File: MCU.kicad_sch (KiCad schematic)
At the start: 101 parts, among them J301 I2C1, J302 I2C4, U301 MICROCONTROLLER, X301 25MHz 8pF

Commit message: starting to incorporate todos
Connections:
- net TX_PWM_A: now also U301.H12 (PD14); no longer U301.F11 (PC7)
- net TX_PWM_B: now also U301.H11 (PD12); no longer U301.D11 (PH14)
- no-connect marks 69 -> 68
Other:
- moved on the sheet: TP357, TP366

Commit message: slight tweaks
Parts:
- added TP304: TP_ROUND_TH_300um, BR_Virtual_Parts:TP_ROUND_SMT_300um, symbol BR_Virtual_Parts:TP_ROUND_SMT_300um
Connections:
- net TX_PWM_A: now also TP357.1, U301.H11 (PD12); no longer TP366.1, U301.H12 (PD14)
- net TX_PWM_B: now also TP366.1, U301.H12 (PD14); no longer TP357.1, U301.H11 (PD12)
- net DEBUG1: now reaches U301.G10 (PD15)
- net DEBUG1: now also TP304.1
- no-connect marks 68 -> 67
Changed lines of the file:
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@@
 	)
 	(junction
+		(at 256.54 332.74)
+		(diameter 0)
+		(color 0 0 0 0)
+	)
+	(junction
 		(at 140.97 46.99)
 		(diameter 0)
@@
 	)
 	(no_connect
-		(at 231.14 332.74)
-	)
-	(no_connect
 		(at 157.48 203.2)
 	)
@@
 	(wire
 		(pts
+			(xy 231.14 332.74) (xy 256.54 332.74)
+		)
+		(stroke
+			(width 0)
+			(type default)
+		)
+	)
+	(wire
+		(pts
 			(xy 167.64 386.08) (xy 170.18 386.08)
 		)
@@
 	(wire
 		(pts
+			(xy 256.54 332.74) (xy 266.7 332.74)
+		)
+		(stroke
+			(width 0)
+			(type default)
+		)
+	)
+	(wire
+		(pts
 			(xy 125.73 353.06) (xy 133.35 353.06)
 		)
@@
 		)
 	)
+	(label "DEBUG1"
+		(at 234.95 332.74 0)
+		(effects
+			(font
+				(size 1.27 1.27)
+			)
+			(justify left bottom)
+		)
+	)
 	(label "MOTOR_VREF"
 		(at 256.54 177.8 180)
@@
 	)
 	(label "TX_PWM_A"
-		(at 234.95 330.2 0)
+		(at 234.95 325.12 0)
 		(effects
 			(font
@@
 	)
 	(label "TX_PWM_B"
-		(at 234.95 325.12 0)
+		(at 234.95 330.2 0)
 		(effects
 			(font
@@
 	(hierarchical_label "TX_PWM_B"
 		(shape output)
-		(at 266.7 325.12 0)
+		(at 266.7 330.2 0)
 		(effects
 			(font
@@
 		)
 	)
+	(hierarchical_label "DEBUG1"
+		(shape output)
+		(at 266.7 332.74 0)
+		(effects
+			(font
+				(size 1.27 1.27)
+			)
+			(justify left)
+		)
+	)
 	(hierarchical_label "TX_PWM_A"
 		(shape output)
-		(at 266.7 330.2 0)
+		(at 266.7 325.12 0)
 		(effects
 			(font
@@
 					(unit 1)
 				)
+			)
+		)
+	)
+	(symbol
+		(lib_id "BR_Virtual_Parts:TP_ROUND_SMT_300um")
+		(at 256.54 332.74 270)
+		(unit 1)
+		(body_style 1)
+		(exclude_from_sim no)
+		(in_bom no)
+		(on_board yes)
+		(in_pos_files yes)
+		(dnp no)
+		(property "Reference" "TP304"
+			(at 259.715 332.74 90)
+			(show_name no)
+			(do_not_autoplace no)
+			(effects
+				(font
+					(size 1.27 1.27)
+				)
+				(justify left)
+			)
+		)
+		(property "Value" "TP_ROUND_TH_300um"
+			(at 266.3825 335.788 0)
+			(hide yes)
+			(show_name no)
+			(do_not_autoplace no)
+			(effects
+				(font
+					(size 1.27 1.27)
+				)
+				(justify left)
+			)
+		)
+		(property "Footprint" "BR_Virtual_Parts:TP_ROUND_SMT_300um"
+			(at 263.906 334.01 0)
+			(hide yes)
+			(show_name no)
+			(do_not_autoplace no)
+			(effects
+				(font
+					(size 1.27 1.27)
+				)
+			)
+		)
+		(property "Datasheet" ""
+			(at 264.033 332.994 0)
+			(hide yes)
+			(show_name no)
+			(do_not_autoplace no)
+			(effects
+				(font
+					(size 1.27 1.27)
+				)
+			)
+		)
+		(property "Description" "test pad surface mount"
+			(at 267.97 333.248 0)
+			(hide yes)
+			(show_name no)
+			(do_not_autoplace no)
+			(effects
+				(font
+					(size 1.27 1.27)
+				)
+			)
+		)
+		(property "Manufacturer" ""
+			(at 264.541 331.216 0)
+			(hide yes)
+			(show_name no)
+			(do_not_autoplace no)
+			(effects
+				(font
+					(size 1.27 1.27)
+				)
+			)
+		)
+		(property "Manufacturer Part Num" ""
+			(at 263.652 332.486 0)
+			(hide yes)
+			(show_name no)
+			(do_not_autoplace no)
+			(effects
+				(font
+					(size 1.27 1.27)
+				)
+			)
+		)
+		(property "Supplier 1" ""
+			(at 264.16 330.835 0)
+			(hide yes)
+			(show_name no)
+			(do_not_autoplace no)
+			(effects
+				(font
+					(size 1.27 1.27)
+				)
+			)
+		)
+		(property "Supplier Part Num 1" ""
+			(at 264.16 331.597 0)
+			(hide yes)
+			(show_name no)
+			(do_not_autoplace no)
+			(effects
+				(font
+					(size 1.27 1.27)
+				)
+			)
+		)
+		(property "Supplier 2" ""
+			(at 263.652 331.47 0)
+			(hide yes)
+			(show_name no)
+			(do_not_autoplace no)
+			(effects
+				(font
+					(size 1.27 1.27)
+				)
+			)
+		)
+		(property "Supplier Part Num 2" ""
+			(at 264.16 332.867 0)
+			(hide yes)
+			(show_name no)
+			(do_not_autoplace no)
+			(effects
+				(font
+					(size 1.27 1.27)
+				)
+			)
+		)
+		(property "Supplier 3" ""
+			(at 264.668 336.296 0)
+			(hide yes)
+			(show_name no)
+			(do_not_autoplace no)
+			(effects
+				(font
+					(size 1.27 1.27)
+				)
+			)
+		)
+		(property "Supplier Part Num 3" ""
+			(at 267.208 338.074 0)
+			(hide yes)
+			(show_name no)
+			(do_not_autoplace no)
+			(effects
+				(font
+					(size 1.27 1.27)
+				)
+			)
+		)
+		(property "BR ID" ""
+			(at 256.54 332.74 0)
+			(hide yes)
+			(show_name no)
+			(do_not_autoplace no)
+			(effects
+				(font
+					(size 1.27 1.27)
+				)
+			)
+		)
+		(pin "1"
+		)
+		(instances
+			(project "PingDevKit"
+				(path "/2a5ce3ef-537a-4122-a1be-ef76186bc0d7/ee0d6f49-3c42-47fb-a769-1c20ea80e0b3"
+					(reference "TP304")
+					(unit 1)
+				)

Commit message: more work
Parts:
- C304, C306, C309, C311, C312, C314, C315, C317, C318, C319, C320, C321, C322, C323, C324, C325: symbol BR_Capacitors_0201:C_0201_100nF_25V_X7R_10% -> BR_Capacitors_0201:C_0201_100nF_25V_X5R_10%
- J301: value I2C1 -> LABEL
- J302: value I2C4 -> LABEL
- L301: value 2u2H 2.2A -> 2u2H 2.7A; JLCPCB Part Num C46527037 -> C54350326; Manufacturer Linepri -> YOUCHI; Manufacturer Part Num LMSC20120652R2MTA -> HCTC-201210-2R2-M
- U301: value MICROCONTROLLER -> STM32H563AII3Q
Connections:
- net SD0 renamed DTX_SD
- net SD1 renamed GPIO_G3
- no-connect marks 67 -> 68
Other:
- moved on the sheet: R301

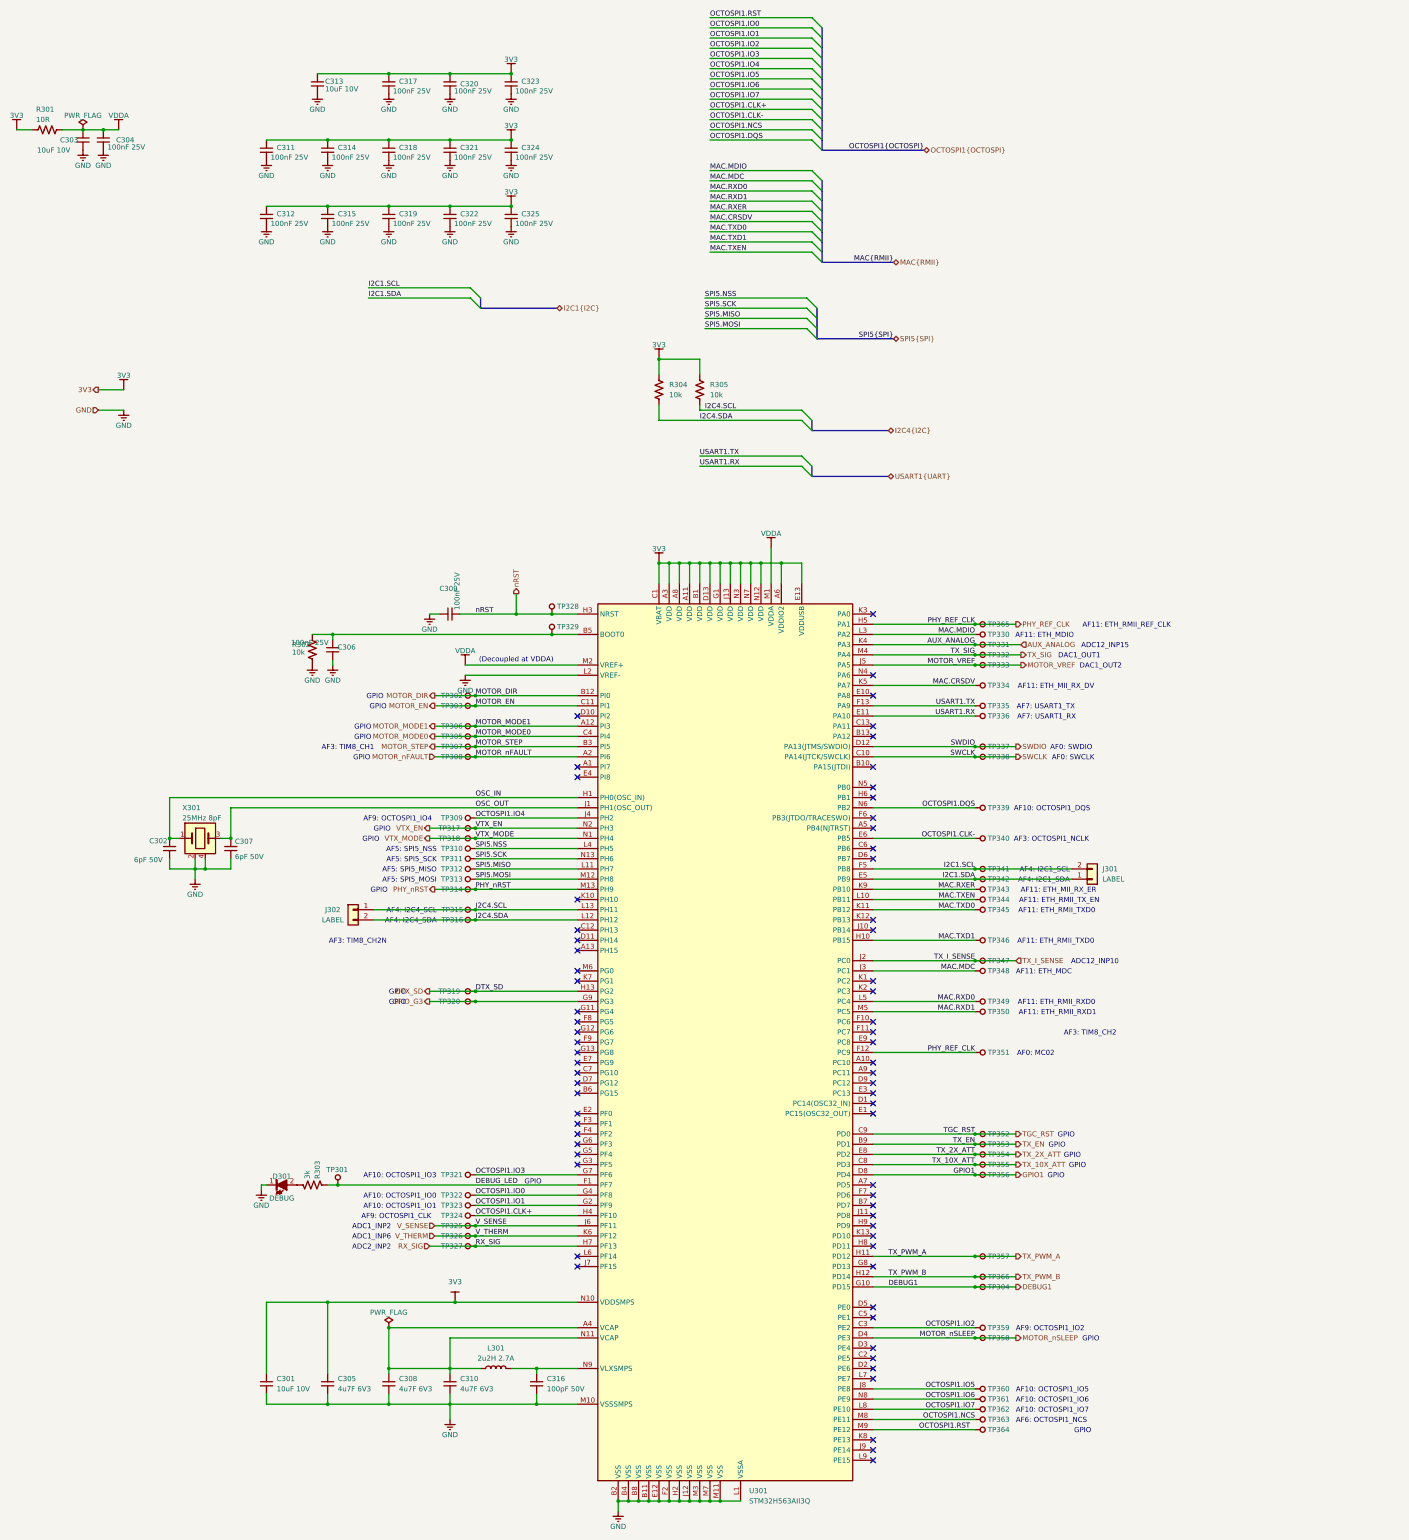
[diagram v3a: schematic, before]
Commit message: refactoring interconnects to simplify busses
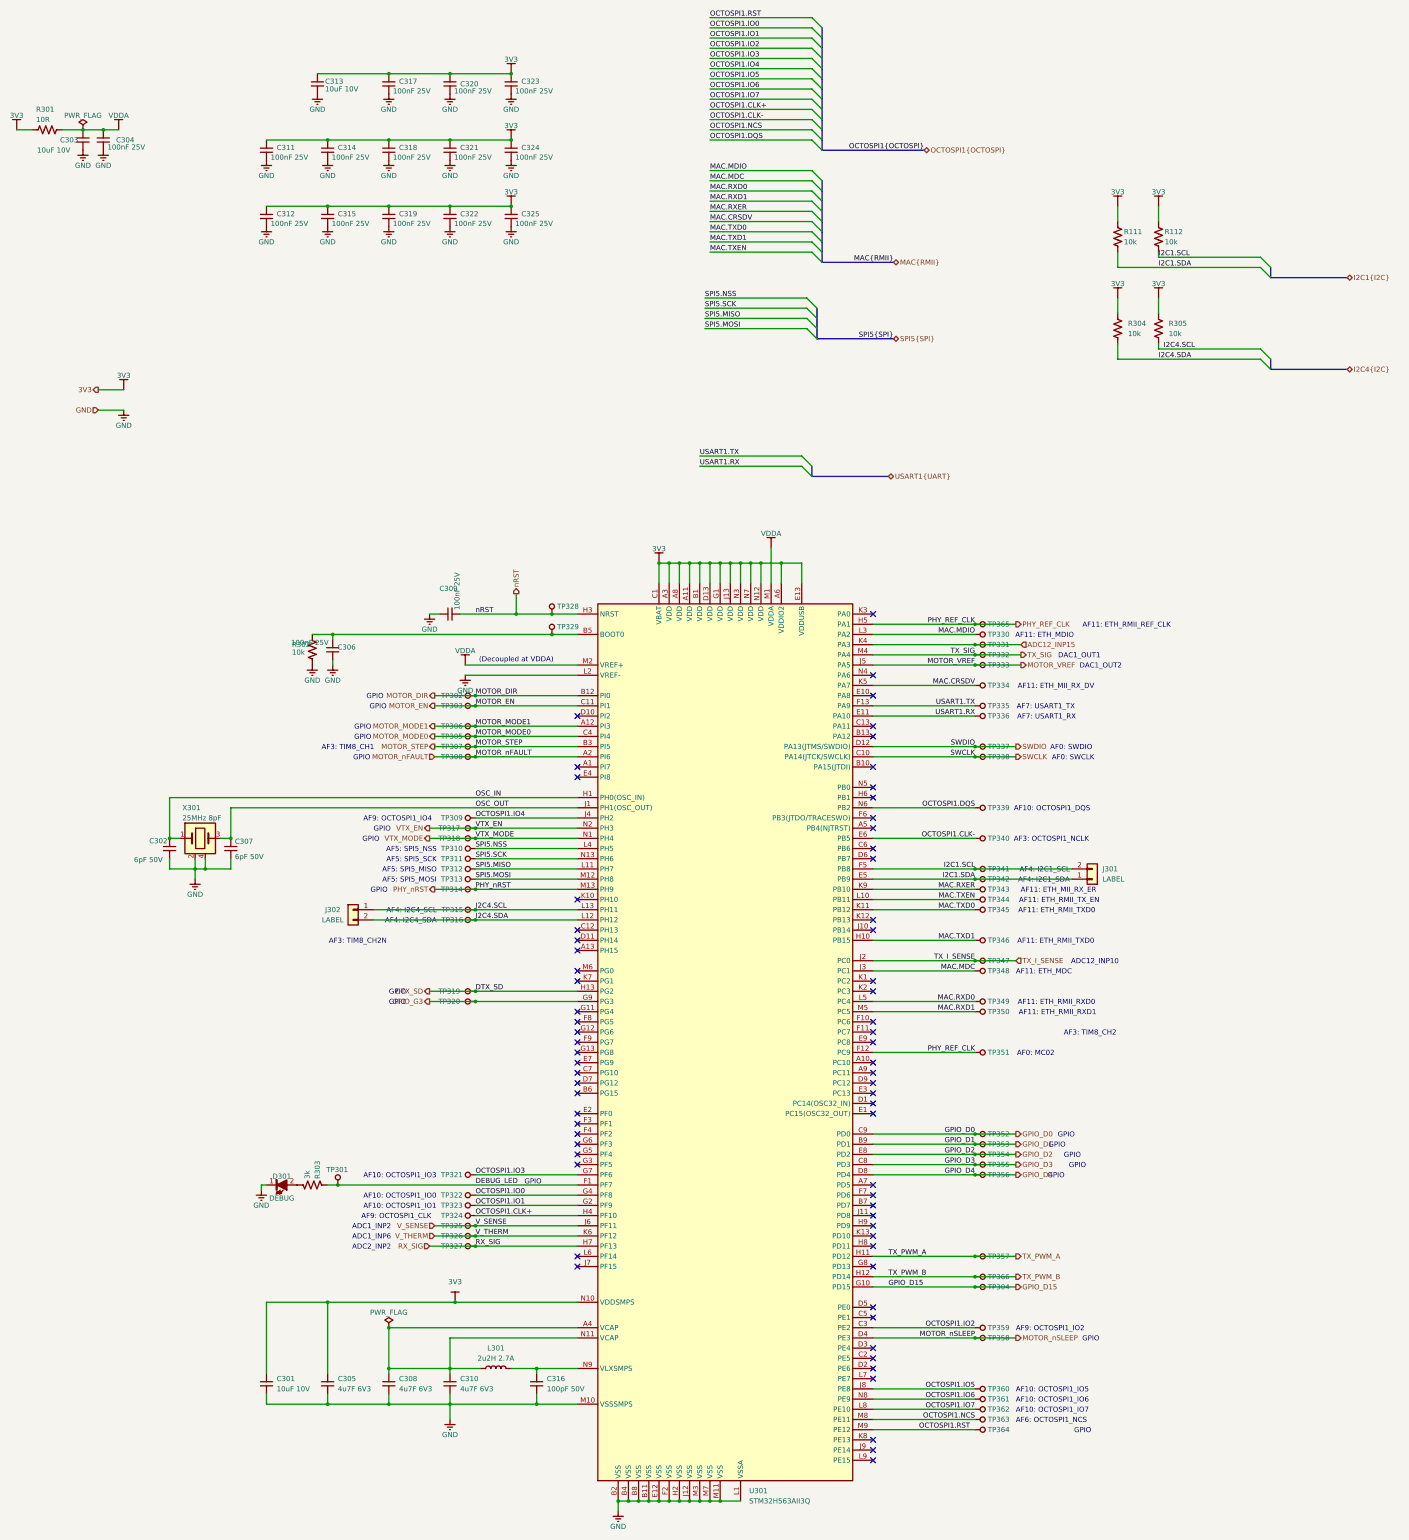
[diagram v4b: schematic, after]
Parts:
- added R111, R112: 10k, BR_Passives:R_0201_0603Metric-minimized, symbol BR_Resistors_0201:R_0201_10k
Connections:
- net 3V3: now also R111.1, R112.1
- net I2C1.SCL: now also R112.2
- net I2C1.SDA: now also R111.2
- net AUX_ANALOG renamed ADC12_INP15
- net DEBUG1 renamed GPIO_D15
- net GPIO1 renamed GPIO_D4
- net TGC_RST renamed GPIO_D0
- net TX_10X_ATT renamed GPIO_D3
- net TX_2X_ATT renamed GPIO_D2
- net TX_EN renamed GPIO_D1
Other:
- note removed: "ADC12_INP15"
- moved on the sheet: R304, R305

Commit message: more work
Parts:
- added TP367: TP_ROUND_TH_300um, BR_Virtual_Parts:TP_ROUND_SMT_300um, symbol BR_Virtual_Parts:TP_ROUND_SMT_300um
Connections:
- net GPIO_I8: now reaches U301.E4 (PI8)
- net GPIO_I8: now also TP358.1
- net ADC12_INP3: now reaches U301.N4 (PA6)
- net ADC12_INP3: now also TP367.1
- net DTX_SD renamed GPIO_G2
- net MOTOR_DIR renamed GPIO_I0
- net MOTOR_EN renamed GPIO_I1
- net MOTOR_MODE0 renamed GPIO_I4
- net MOTOR_MODE1 renamed GPIO_I3
- net MOTOR_STEP renamed GPIO_I5
- net MOTOR_VREF renamed DAC1_OUT2
- net MOTOR_nFAULT renamed GPIO_I6
- net MOTOR_nSLEEP: no longer names the net of U301.D4 (PE3)
- net MOTOR_nSLEEP: no longer TP358.1
- net RX_SIG renamed ADC2_INP2
- net TX_I_SENSE renamed ADC12_INP10
- net TX_PWM_A renamed GPIO_D12
- net TX_PWM_B renamed GPIO_D14
- net TX_SIG renamed DAC1_OUT1
- net V_SENSE renamed ADC1_INP2
- net V_THERM renamed ADC1_INP6
- no-connect marks 68 -> 66
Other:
- note removed: "ADC12_INP10"
- note removed: "ADC1_INP2"
- note removed: "ADC1_INP6"
- note removed: "ADC2_INP2"
- note removed: "DAC1_OUT1"
- note removed: "DAC1_OUT2"
- moved on the sheet: TP358

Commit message: more work
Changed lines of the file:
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@@
 		)
 	)
-	(label "DTX_SD"
+	(label "TX_DSD"
 		(at 132.08 259.08 0)
 		(effects

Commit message: more work
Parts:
- removed D301: DEBUG, BR_Optoelectronics:LED_0603_1608Metric, symbol BR_Optoelectronic:ORH-G36G
- removed R303: 3k, BR_Passives:R_0201_0603Metric-minimized, symbol BR_Resistors_0201:R_0201_3k
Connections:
- net DEBUG_LED renamed GPIO_F7
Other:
- moved on the sheet: TP301

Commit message: more work
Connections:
- net PHY_nRST renamed GPIO_H9
- net VTX_EN renamed GPIO_H3
- net VTX_MODE renamed GPIO_H4
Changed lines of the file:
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@@
 		)
 	)
-	(text "GPIO"
-		(exclude_from_sim no)
-		(at 144.272 307.34 0)
-		(effects
-			(font
-				(size 1.27 1.27)
-			)
-			(justify left bottom)
-		)
-	)
 	(text "AF5: SPI5_SCK"
 		(exclude_from_sim no)
@@
 	(text "GPIO"
 		(exclude_from_sim no)
-		(at 105.918 234.696 0)
-		(effects
-			(font
-				(size 1.27 1.27)
-			)
-			(justify left bottom)
-		)
-	)
-	(text "GPIO"
-		(exclude_from_sim no)
 		(at 278.638 300.736 0)
 		(effects
@@
 		)
 	)
-	(text "GPIO"
-		(exclude_from_sim no)
-		(at 103.886 221.996 0)
-		(effects
-			(font
-				(size 1.27 1.27)
-			)
-			(justify left bottom)
-		)
-	)
 	(text "AF11: ETH_MII_RX_ER"
 		(exclude_from_sim no)
@@
 		)
 	)
-	(text "GPIO"
-		(exclude_from_sim no)
-		(at 106.68 219.456 0)
-		(effects
-			(font
-				(size 1.27 1.27)
-			)
-			(justify left bottom)
-		)
-	)
 	(text "AF10: OCTOSPI1_IO6\n"
 		(exclude_from_sim no)
@@
 	)
 	(bus_entry
+		(at 215.9 52.07)
+		(size 2.54 2.54)
+		(stroke
+			(width 0)
+			(type default)
+		)
+	)
+	(bus_entry
 		(at 215.9 41.91)
 		(size 2.54 2.54)
@@
 		)
 	)
+	(bus
+		(pts
+			(xy 218.44 54.61) (xy 218.44 57.15)
+		)
+		(stroke
+			(width 0)
+			(type default)
+		)
+	)
 	(wire
 		(pts
@@
 	(wire
 		(pts
+			(xy 190.5 52.07) (xy 215.9 52.07)
+		)
+		(stroke
+			(width 0)
+			(type default)
+		)
+	)
+	(wire
+		(pts
 			(xy 120.65 307.34) (xy 132.08 307.34)
 		)
@@
 	)
 	(label "ADC2_INP2"
-		(at 132.08 322.58 0)
+		(at 133.35 322.58 0)
 		(effects
 			(font
@@
 	)
 	(label "SPI5.NSS"
-		(at 132.08 223.52 0)
+		(at 133.35 223.52 0)
 		(effects
 			(font
@@
 	)
 	(label "VTX_EN"
-		(at 132.08 218.44 0)
+		(at 133.35 218.44 0)
 		(effects
 			(font
@@
 	)
 	(label "MOTOR_STEP"
-		(at 132.08 198.12 0)
+		(at 133.35 198.12 0)
 		(effects
 			(font
@@
 	)
 	(label "MOTOR_MODE1"
-		(at 132.08 193.04 0)
+		(at 133.35 193.04 0)
 		(effects
 			(font
@@
 	)
 	(label "I2C4.SCL"
-		(at 132.08 238.76 0)
+		(at 133.35 238.76 0)
 		(effects
 			(font
@@
 	)
 	(label "OCTOSPI1.IO0"
-		(at 132.08 309.88 0)
+		(at 133.35 309.88 0)
 		(effects
 			(font
@@
 	)
 	(label "OCTOSPI1.IO3"
-		(at 132.08 304.8 0)
+		(at 133.35 304.8 0)
 		(effects
 			(font
@@
 	)
 	(label "V_THERM"
-		(at 132.08 320.04 0)
+		(at 133.35 320.04 0)
 		(effects
 			(font
@@
 	)
 	(label "SPI5.MISO"
-		(at 132.08 228.6 0)
+		(at 133.35 228.6 0)
 		(effects
 			(font
@@
 	)
 	(label "OCTOSPI1.IO1"
-		(at 132.08 312.42 0)
+		(at 133.35 312.42 0)
 		(effects
 			(font
@@
 	)
 	(label "OCTOSPI1.CLK+"
-		(at 132.08 314.96 0)
+		(at 133.35 314.96 0)
 		(effects
 			(font
@@
 	)
 	(label "OSC_OUT"
-		(at 132.08 213.36 0)
+		(at 133.35 213.36 0)
 		(effects
 			(font
@@
 		)
 	)
-	(label "PHY_REF_CLK"
+	(label "MAC.REF_CLK"
 		(at 256.54 167.64 180)
 		(effects
@@
 	)
 	(label "TX_DSD"
-		(at 132.08 259.08 0)
+		(at 133.35 259.08 0)
 		(effects
 			(font
@@
 	)
 	(label "MOTOR_DIR"
-		(at 132.08 185.42 0)
+		(at 133.35 185.42 0)
 		(effects
 			(font
@@
 	)
 	(label "SPI5.SCK"
-		(at 132.08 226.06 0)
+		(at 133.35 226.06 0)
 		(effects
 			(font
@@
 	)
 	(label "MOTOR_MODE0"
-		(at 132.08 195.58 0)
+		(at 133.35 195.58 0)
 		(effects
 			(font
@@
 	)
 	(label "DEBUG_LED"
-		(at 132.08 307.34 0)
+		(at 133.35 307.34 0)
 		(effects
 			(font
@@
 	)
 	(label "I2C4.SDA"
-		(at 132.08 241.3 0)
+		(at 133.35 241.3 0)
 		(effects
 			(font
@@
 	)
 	(label "MOTOR_nFAULT"
-		(at 132.08 200.66 0)
+		(at 133.35 200.66 0)
 		(effects
 			(font
@@
 	)
 	(label "SPI5.MOSI"
-		(at 132.08 231.14 0)
+		(at 133.35 231.14 0)
 		(effects
 			(font
@@
 	)
 	(label "MOTOR_nSLEEP"
-		(at 132.08 205.74 0)
+		(at 133.35 205.74 0)
 		(effects
 			(font
@@
 	)
 	(label "OCTOSPI1.IO4"
-		(at 132.08 215.9 0)
+		(at 133.35 215.9 0)
 		(effects
 			(font
@@
 		)
 	)
-	(label "GPIO_D3"
-		(at 256.54 302.26 180)
+	(label "MAC.REF_CLK"
+		(at 190.5 52.07 0)
 		(effects
 			(font
 				(size 1.27 1.27)
 			)
-			(justify right bottom)
+			(justify left bottom)
 		)
 	)
-	(label "PHY_nRST"
-		(at 132.08 233.68 0)
+	(label "GPIO_D3"
+		(at 256.54 302.26 180)
 		(effects
 			(font
 				(size 1.27 1.27)
 			)
-			(justify left bottom)
+			(justify right bottom)
 		)
 	)
-	(label "OCTOSPI1.IO5"
-		(at 190.5 31.75 0)
+	(label "PHY_nRST"
+		(at 133.35 233.68 0)
 		(effects
 			(font
@@
 		)
 	)
-	(label "VTX_MODE"
-		(at 132.08 220.98 0)
+	(label "OCTOSPI1.IO5"
+		(at 190.5 31.75 0)
 		(effects
 			(font
@@
 	)
 	(label "MOTOR_EN"
-		(at 132.08 187.96 0)
+		(at 133.35 187.96 0)
 		(effects
 			(font
@@
 	)
 	(label "OSC_IN"
-		(at 132.08 210.82 0)
+		(at 133.35 210.82 0)
 		(effects
 			(font
@@
 		)
 	)
-	(hierarchical_label "VTX_MODE"
+	(hierarchical_label "GPIO_H4"
 		(shape output)
 		(at 120.65 220.98 180)
@@
 		)
 	)
-	(hierarchical_label "PHY_nRST"
+	(hierarchical_label "GPIO_H9"
 		(shape output)
 		(at 121.92 233.68 180)
@@
 		)
 	)
-	(hierarchical_label "VTX_EN"
+	(hierarchical_label "GPIO_H3"
 		(shape output)
 		(at 120.65 218.44 180)
